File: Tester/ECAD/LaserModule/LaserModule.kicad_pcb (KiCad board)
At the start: 2 copper layers, 29.2 x 44.4 mm, 14 parts, among them J1 Conn_01x04_Male, Q1 ZXMP6A17G, U1 MCP4716, U2 AD8601

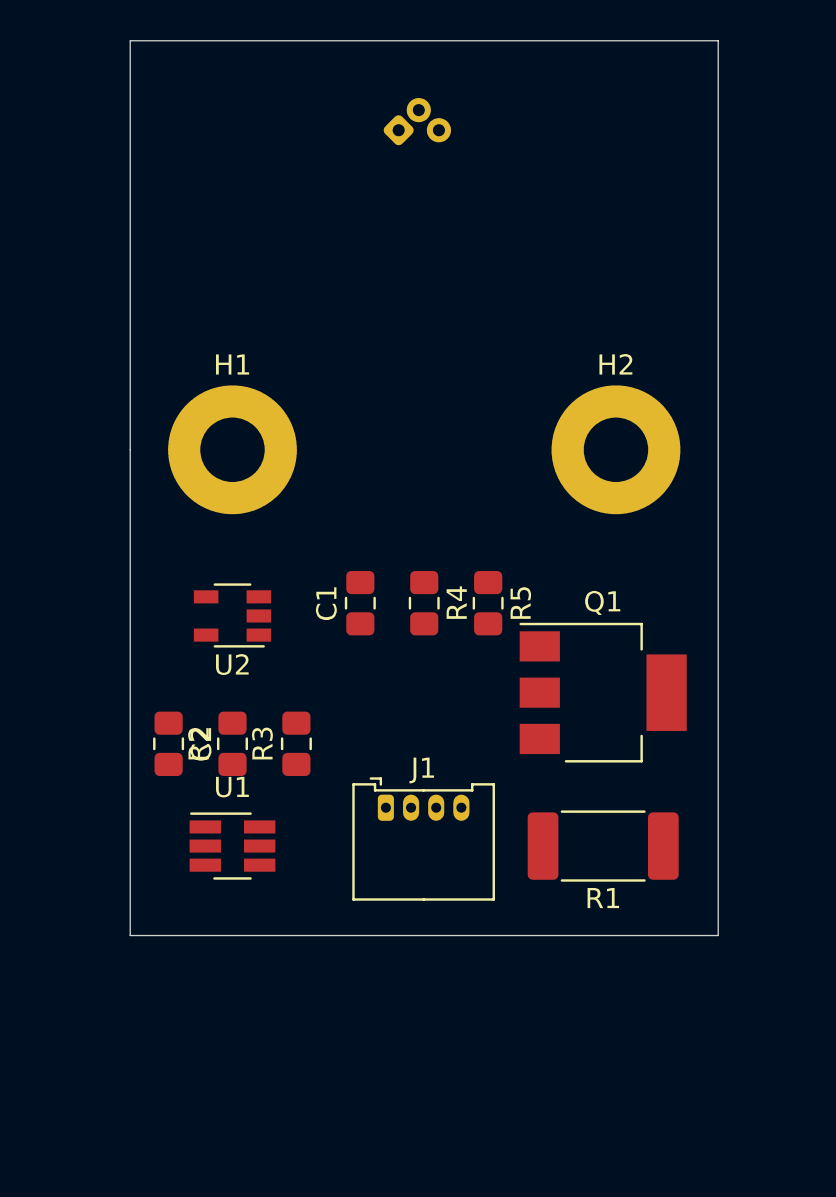
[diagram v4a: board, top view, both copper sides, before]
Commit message: Progressed laser module layout.
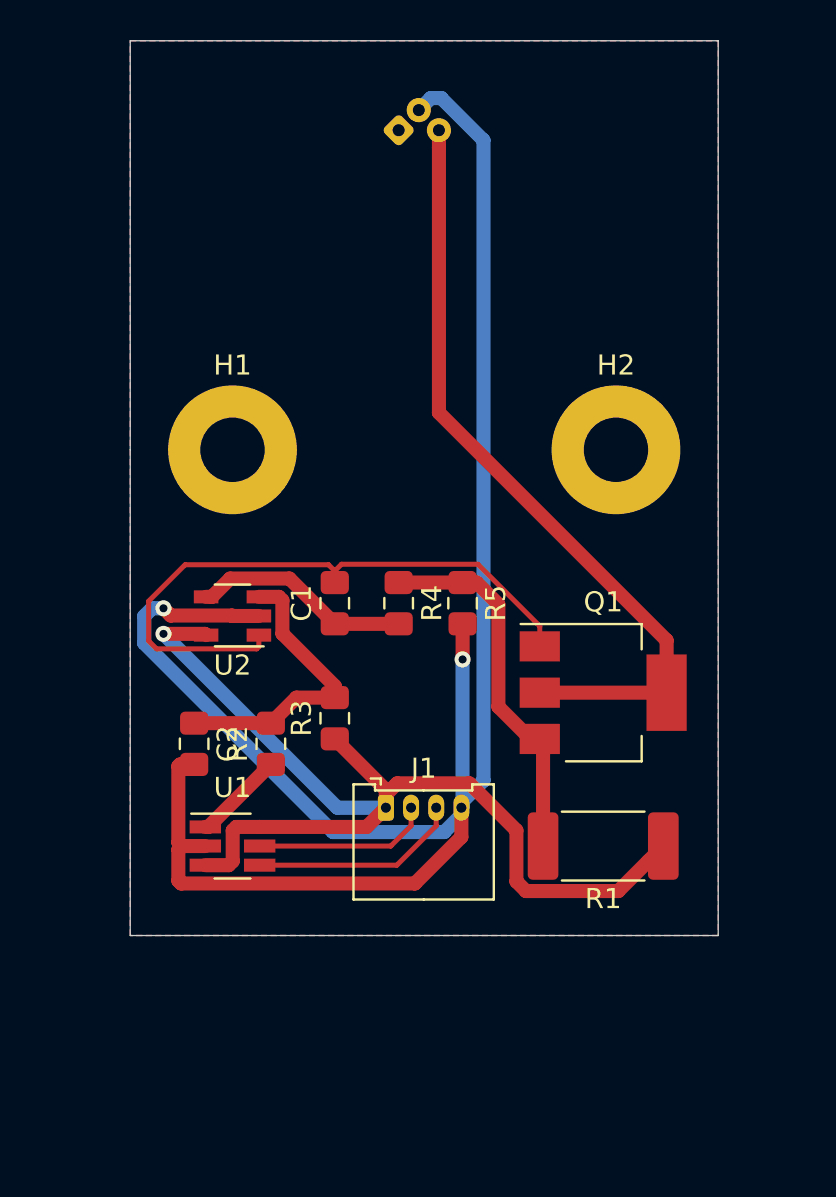
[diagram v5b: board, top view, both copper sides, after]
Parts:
- moved R3 2.29 mm to (138.4, 81.9)
- moved R2 1.91 mm to (135.3, 83.2)
- moved R4 1.27 mm to (141.6, 76.2)
- moved R5 1.27 mm to (144.8, 76.2)
- moved C1 1.27 mm to (138.4, 76.2)
- moved C2 1.27 mm to (131.4, 83.2)
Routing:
- net GND: track 0.00 -> 99.2 mm, vias 0 -> 2
- net +5C: track 0.00 -> 51.6 mm, vias 0 -> 1
- net /D: track 0.00 -> 38.9 mm
- net /G: track 0.00 -> 31.5 mm
- net /S: track 0.00 -> 18.6 mm
- net /V+: track 0.00 -> 14.7 mm
- net /V-: track 0.00 -> 10.9 mm
- net /SDA: track 0.00 -> 10.5 mm
- net /SCL: track 0.00 -> 8.84 mm
- net /VOUT: track 0.00 -> 4.54 mm
- added copper zone on F.Cu, net +5C
- added copper zone on B.Cu, net GND

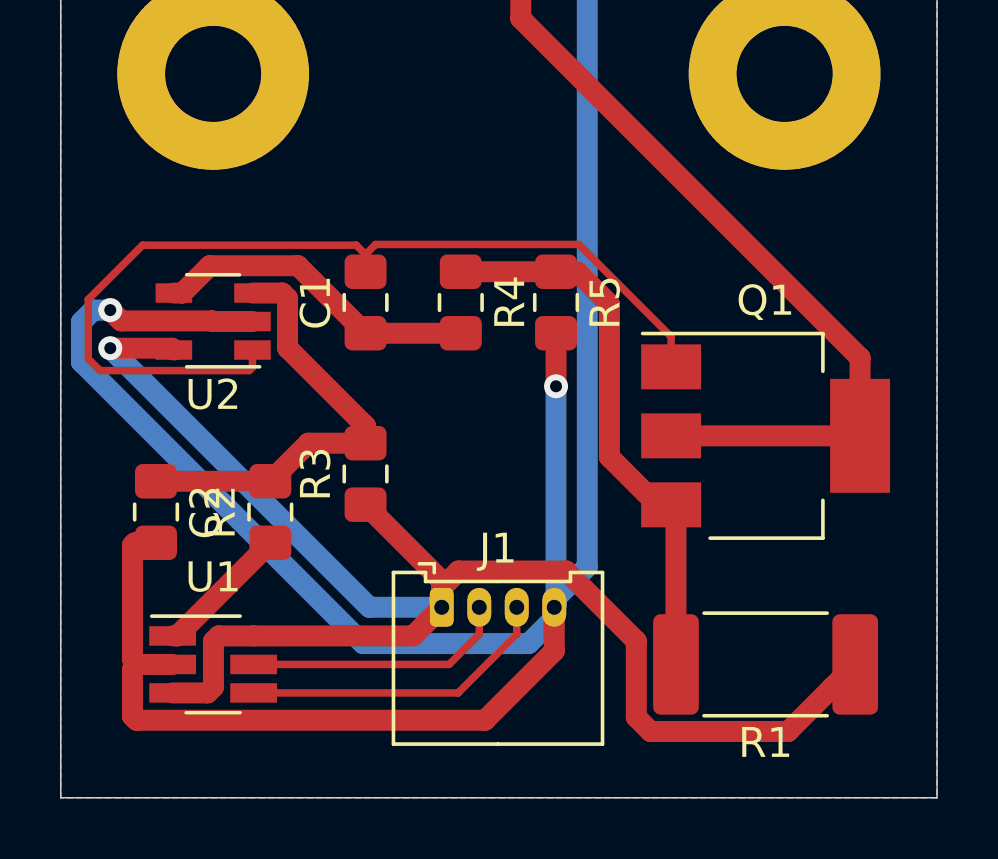
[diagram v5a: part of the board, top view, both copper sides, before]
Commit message: Generated laser module gerbers.
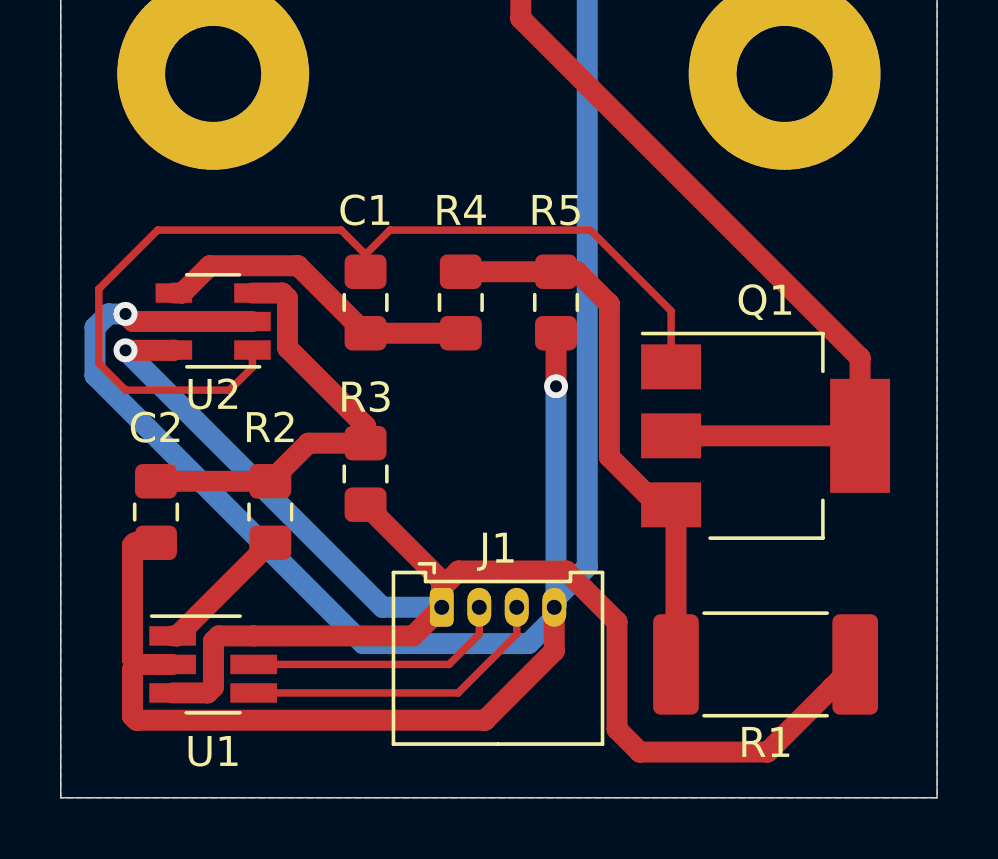
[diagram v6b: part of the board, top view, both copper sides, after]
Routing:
- net /G: track 31.5 -> 33.0 mm
- net GND: track 99.2 -> 98.3 mm
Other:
- board text added: "Laser Module"
- board text added: "Nuno Sousa 20/02/2020"

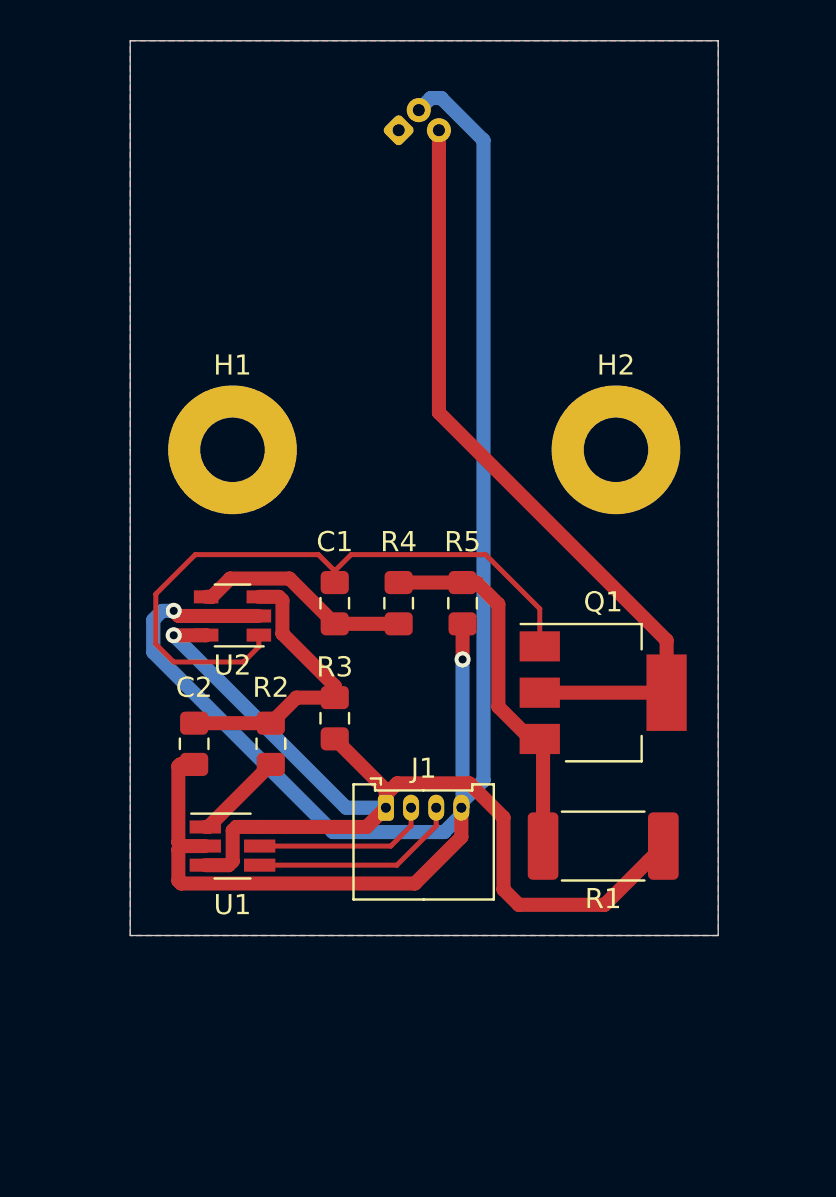
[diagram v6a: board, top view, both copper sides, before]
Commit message: Added solder jumpers.
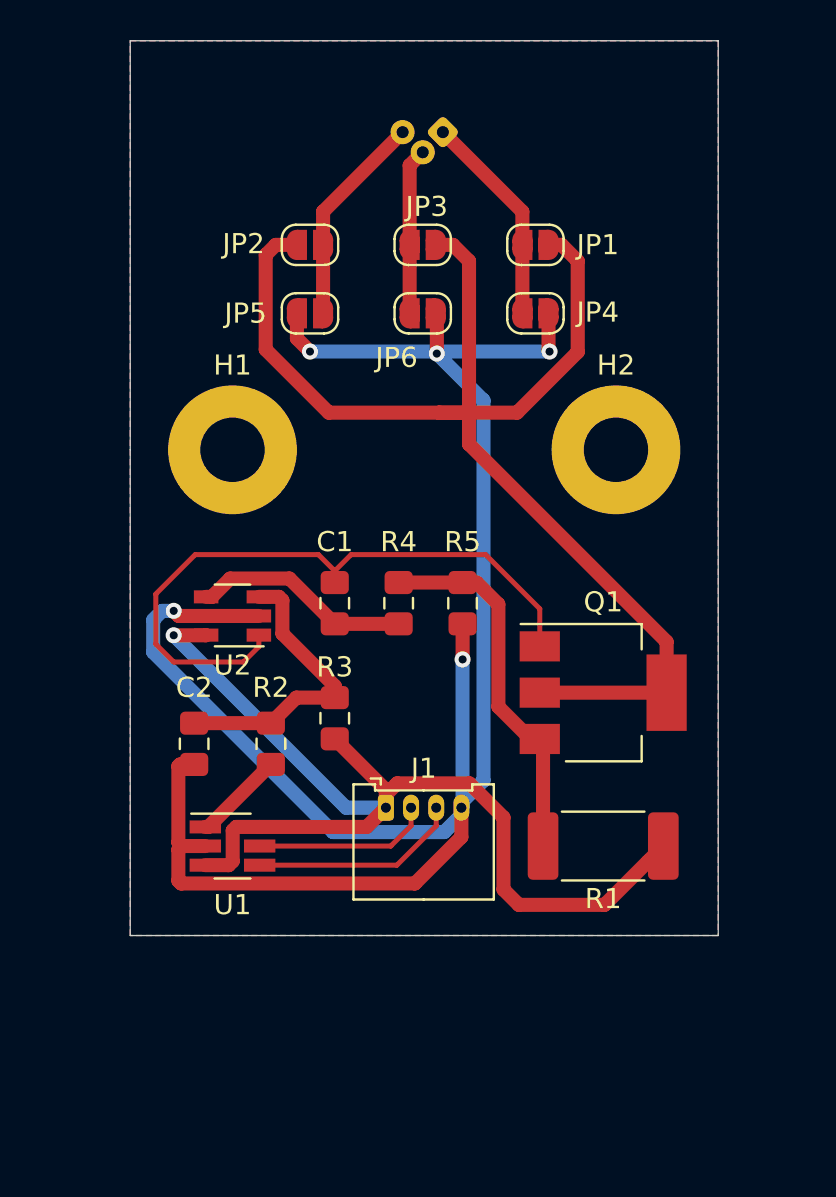
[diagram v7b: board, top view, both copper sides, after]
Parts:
- added JP1: SolderJumper_2_Open, Jumper:SolderJumper-2_P1.3mm_Open_RoundedPad1.0x1.5mm, F.Cu at (148.4, 58.4)
- added JP2: SolderJumper_2_Open, Jumper:SolderJumper-2_P1.3mm_Open_RoundedPad1.0x1.5mm, F.Cu at (137.2, 58.4)
- added JP3: SolderJumper_2_Open, Jumper:SolderJumper-2_P1.3mm_Open_RoundedPad1.0x1.5mm, F.Cu at (142.8, 58.4)
- added JP4: SolderJumper_2_Open, Jumper:SolderJumper-2_P1.3mm_Open_RoundedPad1.0x1.5mm, F.Cu at (148.4, 61.8)
- added JP5: SolderJumper_2_Open, Jumper:SolderJumper-2_P1.3mm_Open_RoundedPad1.0x1.5mm, F.Cu at (137.2, 61.8)
- added JP6: SolderJumper_2_Open, Jumper:SolderJumper-2_P1.3mm_Open_RoundedPad1.0x1.5mm, F.Cu at (142.8, 61.8)
- moved LD1 2.20 mm to (143.8, 52.8), turned to 180 degrees
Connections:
- LD1 pad 2: GND -> Net-(JP3-Pad1)
- LD1 pad 3: /D -> Net-(JP2-Pad1)
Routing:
- net /D: track 38.9 -> 66.1 mm
- net Net-(JP2-Pad1): track 0.00 -> 10.6 mm
- net Net-(JP1-Pad1): track 0.00 -> 10.6 mm
- net Net-(JP3-Pad1): track 0.00 -> 8.27 mm
- net GND: track 98.3 -> 102.4 mm, vias 2 -> 5

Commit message: Added 3D models.
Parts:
- J1: footprint Connector_Molex:Molex_PicoBlade_53048-0410_1x04_P1.25mm_Horizontal -> Connector_Molex_Custom:Molex_PicoBlade_53048-0410_1x04_P1.25mm_Horizontal
